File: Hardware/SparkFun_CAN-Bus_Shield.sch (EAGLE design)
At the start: 48 parts, among them Q1 16MHz, U1 USD-SOCKETNEW, U2 ARDUINO_R3_SHIELD, U3 JST_VERTICAL, U4 MCP2515, U5 MCP2551, U6 HEX_CONVERTER, X1 DB9 Plug

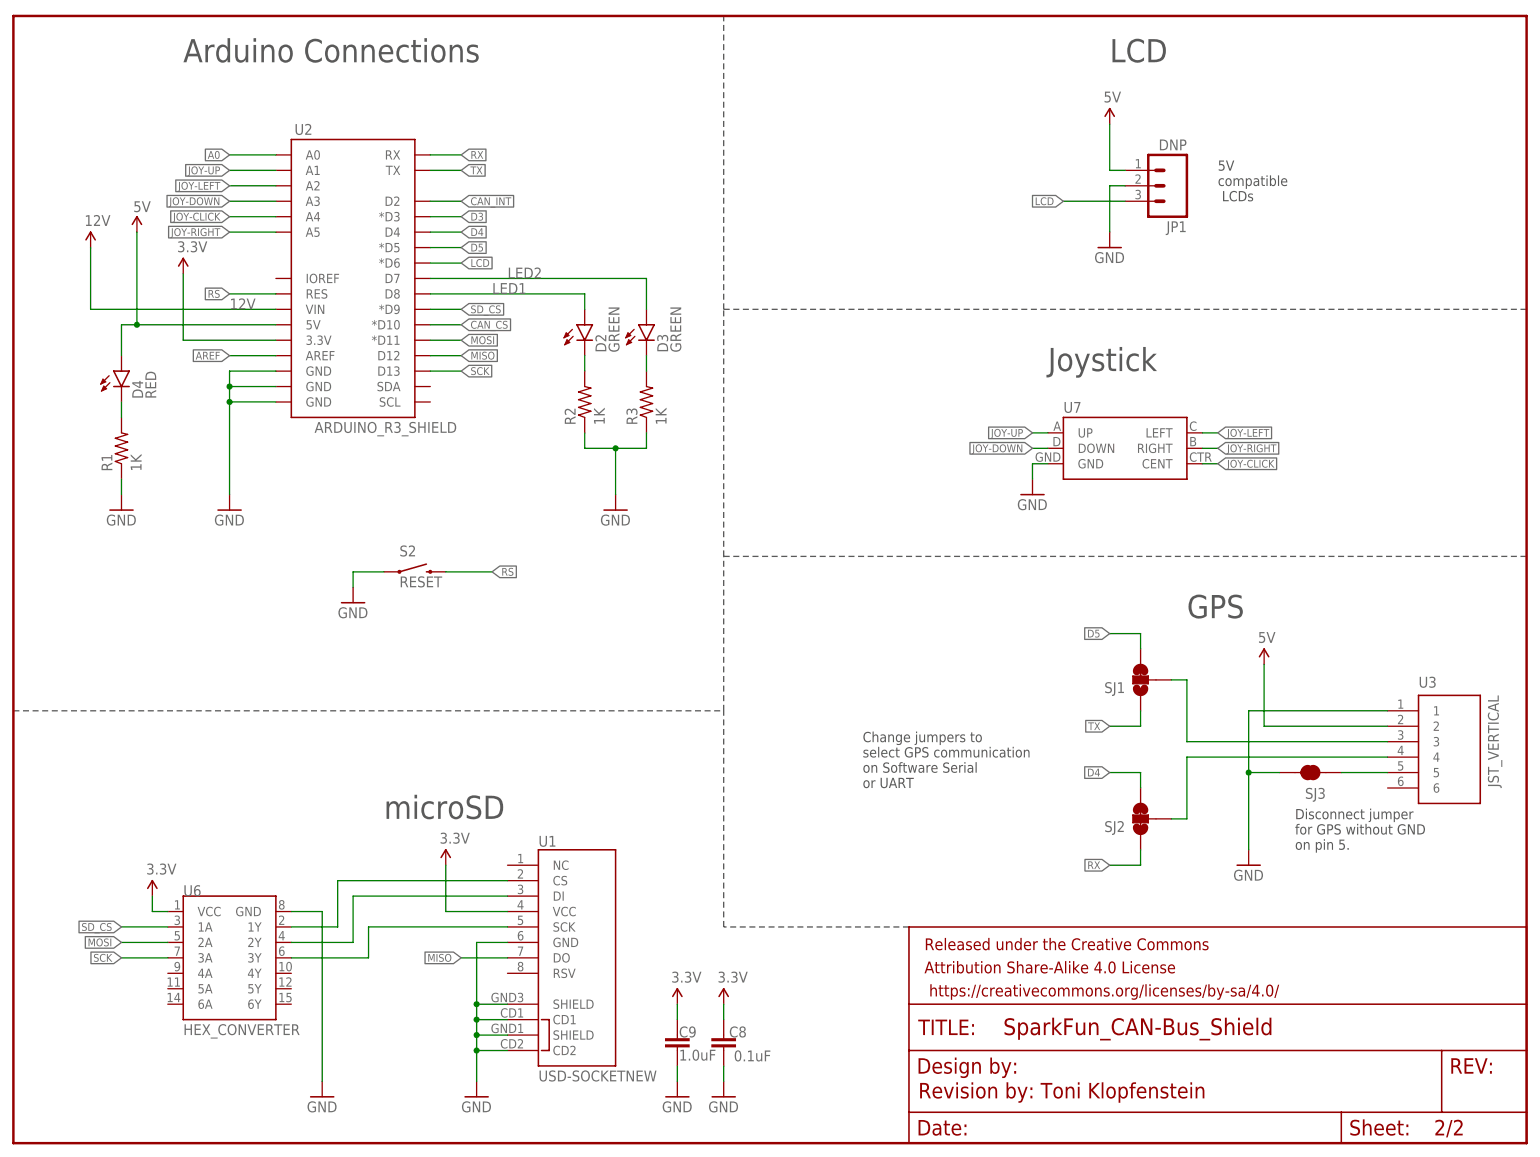
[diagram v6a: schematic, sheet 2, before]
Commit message: Updating to new uSD footprint, minor QC cleanup on schematic
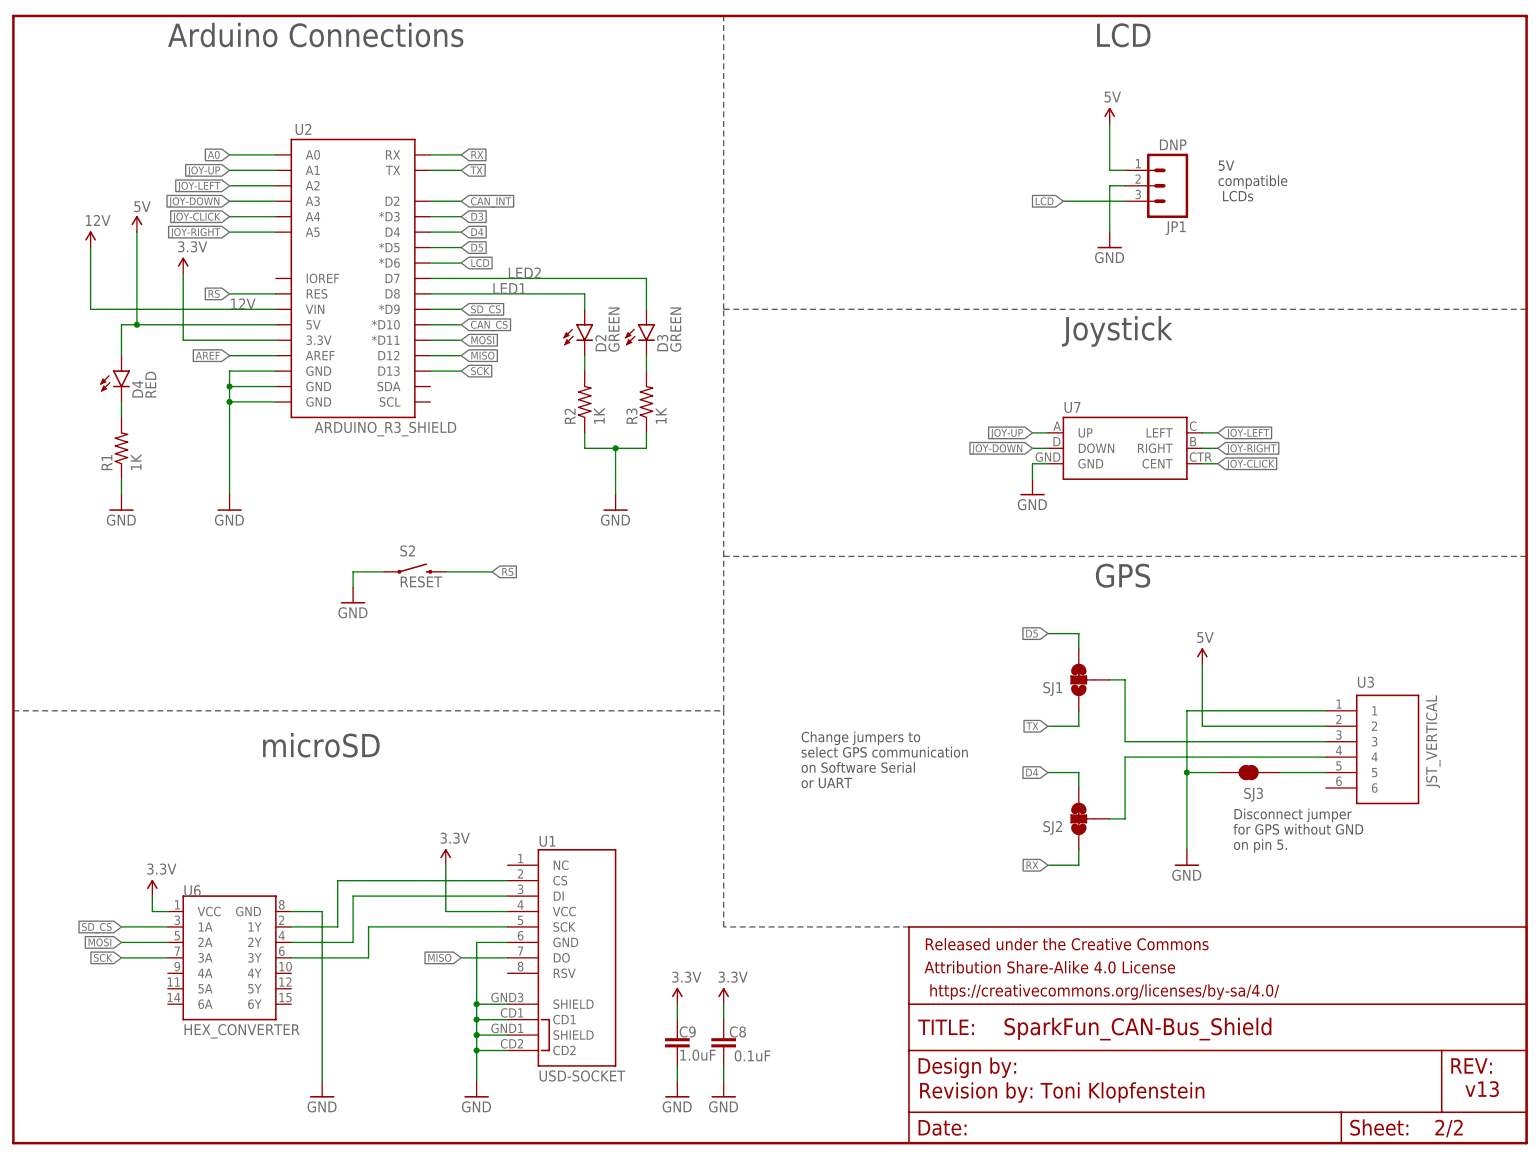
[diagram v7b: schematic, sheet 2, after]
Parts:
- FRAME1: value (none) -> FRAME-LETTER; DESIGNER Sukkin Pang and Ryan Owens -> (none); VERSION v13 -> (none)
- FRAME2: value (none) -> FRAME-LETTERNO_PACKAGE
- U1: value USD-SOCKETNEW -> USD-SOCKET; device SparkFun-Connectors:USD-SOCKETNEW -> SparkFun-Connectors:USD-SOCKET
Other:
- note added: "Sukkin Pang"
- note added: "v13"
- moved on the sheet: SJ1, SJ2, SJ3, U3

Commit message: Updating PESD1CAN part to new library path
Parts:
- D5: device Testing:PESD1CAN -> SparkFun-DiscreteSemi:PESD1CAN
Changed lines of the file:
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@@
 <part name="SJ5" library="SparkFun-Passives" deviceset="JUMPER-PAD-3-2OF3_NC_BY_TRACE" device="_SMALL"/>
 <part name="SJ6" library="SparkFun-Passives" deviceset="JUMPER-PAD-3-2OF3_NC_BY_TRACE" device="_SMALL"/>
-<part name="D5" library="Testing" deviceset="PESD1CAN" device=""/>
+<part name="D5" library="SparkFun-DiscreteSemi" deviceset="PESD1CAN" device=""/>
 <part name="GND20" library="SparkFun-Aesthetics" deviceset="GND" device=""/>
 </parts>
